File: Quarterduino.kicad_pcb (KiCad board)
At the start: 2 copper layers, 34.3 x 26.7 mm, 39 parts, among them CN1 CON_USB-C-16, CN2 CON_AVRISP, P1 Power, P2 Analog, P3 Digital, P4 Digital, Q1 FDN340P, U1 REG_AP7215, U2 LMV358, U3 IC_FT232RQ, U4 ATmega328P-MU, U5 LDO_5p_NJM2865, Y1 Crystal_GND24

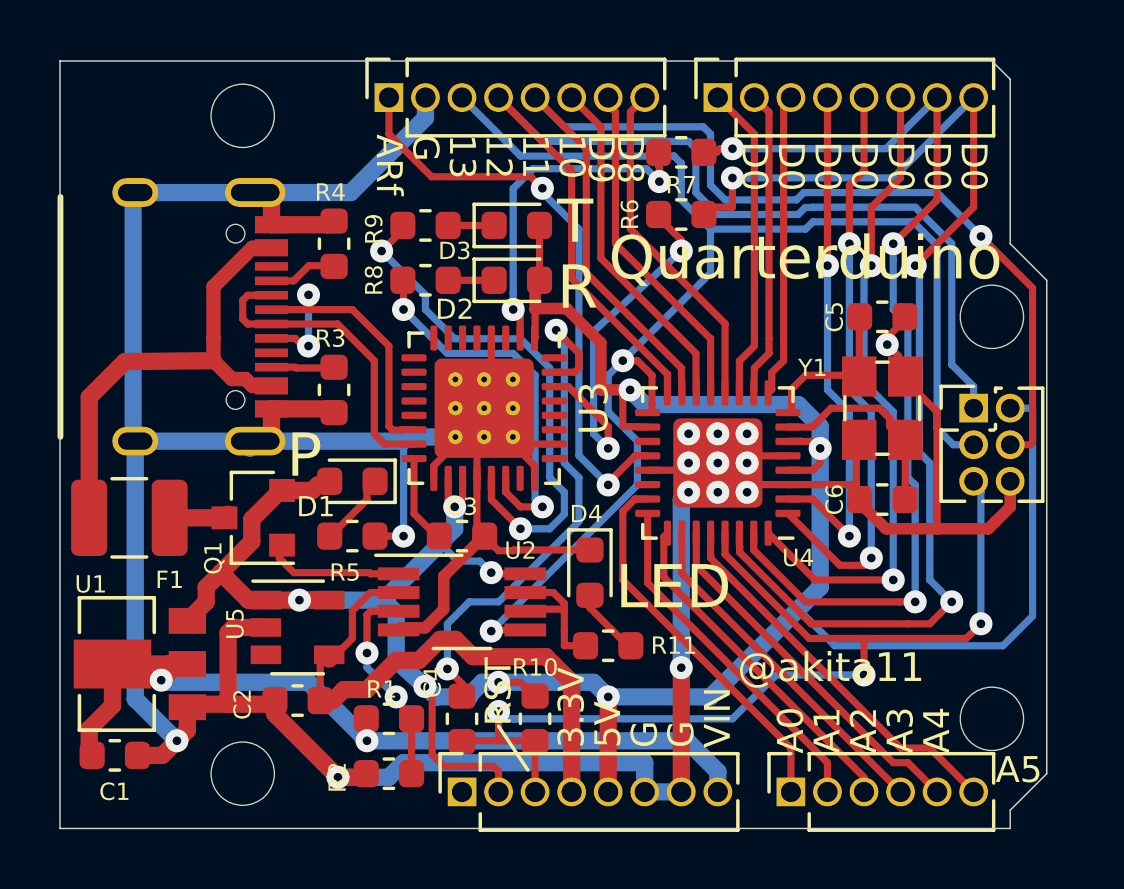
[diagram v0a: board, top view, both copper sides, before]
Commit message: ベタGNDの追加
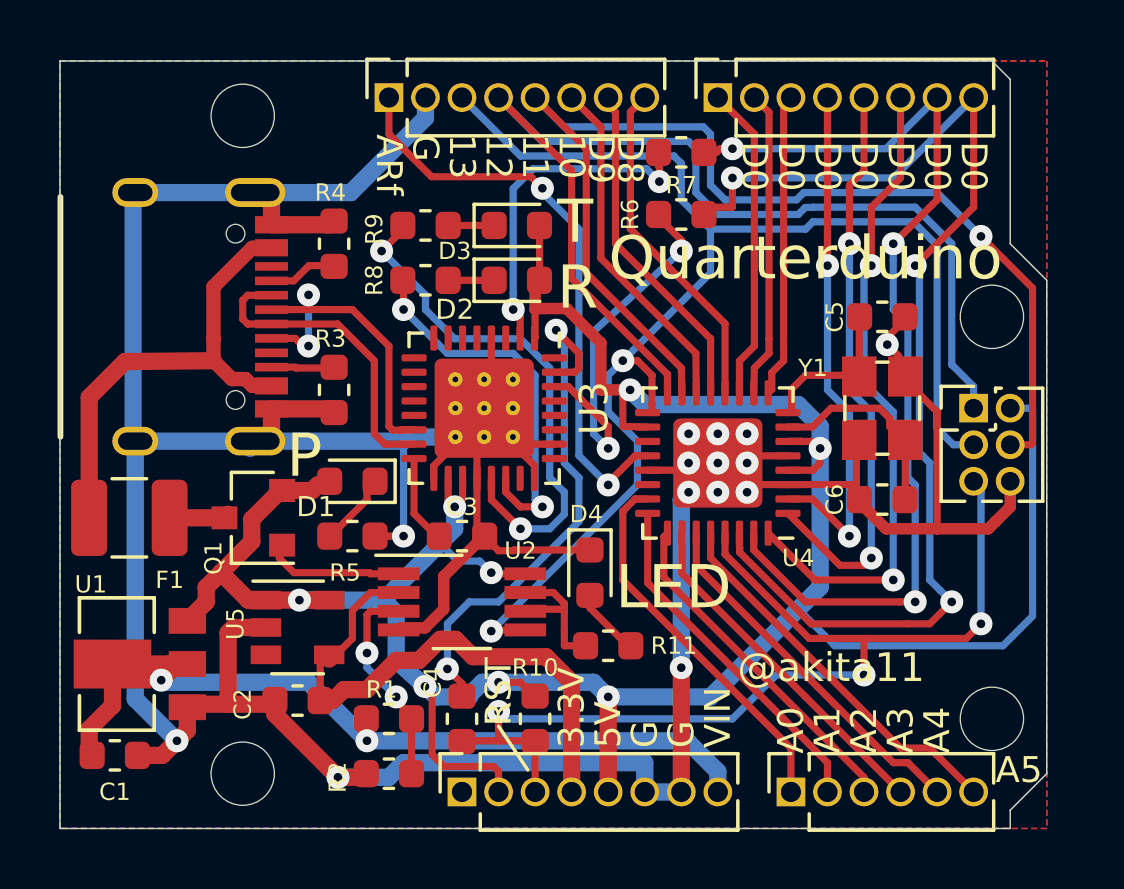
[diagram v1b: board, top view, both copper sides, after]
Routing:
- added copper zone on B.Cu, net GND
- added copper zone on F.Cu, net GND
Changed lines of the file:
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@@
   (layers
     (0 F.Cu signal)
-    (31 B.Cu signal hide)
+    (31 B.Cu signal)
     (32 B.Adhes user hide)
     (33 F.Adhes user hide)
@@
     (solder_mask_min_width 0.25)
     (aux_axis_origin 0 0)
-    (visible_elements FFFFFF7F)
+    (visible_elements 7FFFFFFF)
     (pcbplotparams
       (layerselection 0x010fc_ffffffff)
-      (usegerberextensions false)
+      (usegerberextensions true)
       (usegerberattributes false)
       (usegerberadvancedattributes false)
@@
       (outputformat 1)
       (mirror false)
-      (drillshape 1)
+      (drillshape 0)
       (scaleselection 1)
       (outputdirectory ""))
@@
   (segment (start 6.686554 -15.38) (end 6.449153 -15.617401) (width 0.5) (layer F.Cu) (net 63))
   (segment (start 5.334 -17.018) (end 5.334 -16.256) (width 0.5) (layer F.Cu) (net 63))
+  (zone (net 1) (net_name GND) (layer F.Cu) (hatch edge 0.508)
+    (connect_pads (clearance 0.508))
+    (min_thickness 0.254)
+    (fill yes (arc_segments 32) (thermal_gap 0.508) (thermal_bridge_width 0.508))
+    (polygon
+      (pts
+        (xy 34.29 0) (xy 0 0) (xy 0 -26.67) (xy 34.29 -26.67)
+      )
+    )
+  )
+  (zone (net 1) (net_name GND) (layer F.Cu) (hatch edge 0.508)
+    (connect_pads (clearance 0.508))
+    (min_thickness 0.254)
+    (fill yes (arc_segments 32) (thermal_gap 0.508) (thermal_bridge_width 0.508))
+    (polygon
+      (pts
+        (xy 34.29 0) (xy 0 0) (xy 0 -26.67) (xy 34.29 -26.67)
+      )
+    )
+  )
+  (zone (net 1) (net_name GND) (layer B.Cu) (hatch edge 0.508)
+    (connect_pads (clearance 0.508))
+    (min_thickness 0.254)
+    (fill yes (arc_segments 32) (thermal_gap 0.508) (thermal_bridge_width 0.508))
+    (polygon
+      (pts
+        (xy 34.29 0) (xy 0 0) (xy 0 -26.67) (xy 34.29 -26.67)
+      )
+    )
+  )
 )
